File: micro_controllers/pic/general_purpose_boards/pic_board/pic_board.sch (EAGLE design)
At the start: 26 parts, among them IC1 PIC16f877a, IC2 7805TV

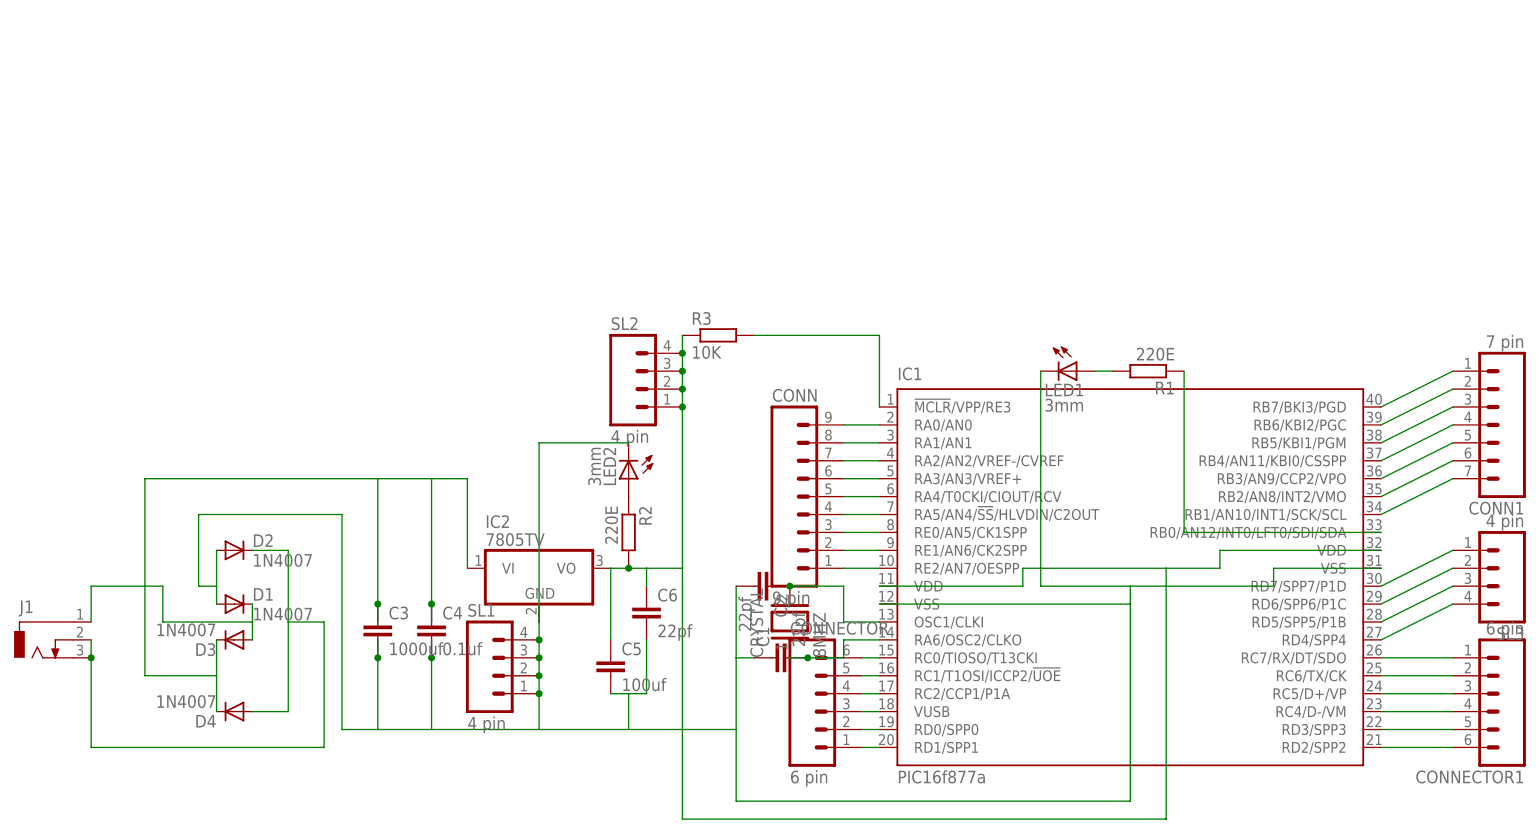
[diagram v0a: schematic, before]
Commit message: 
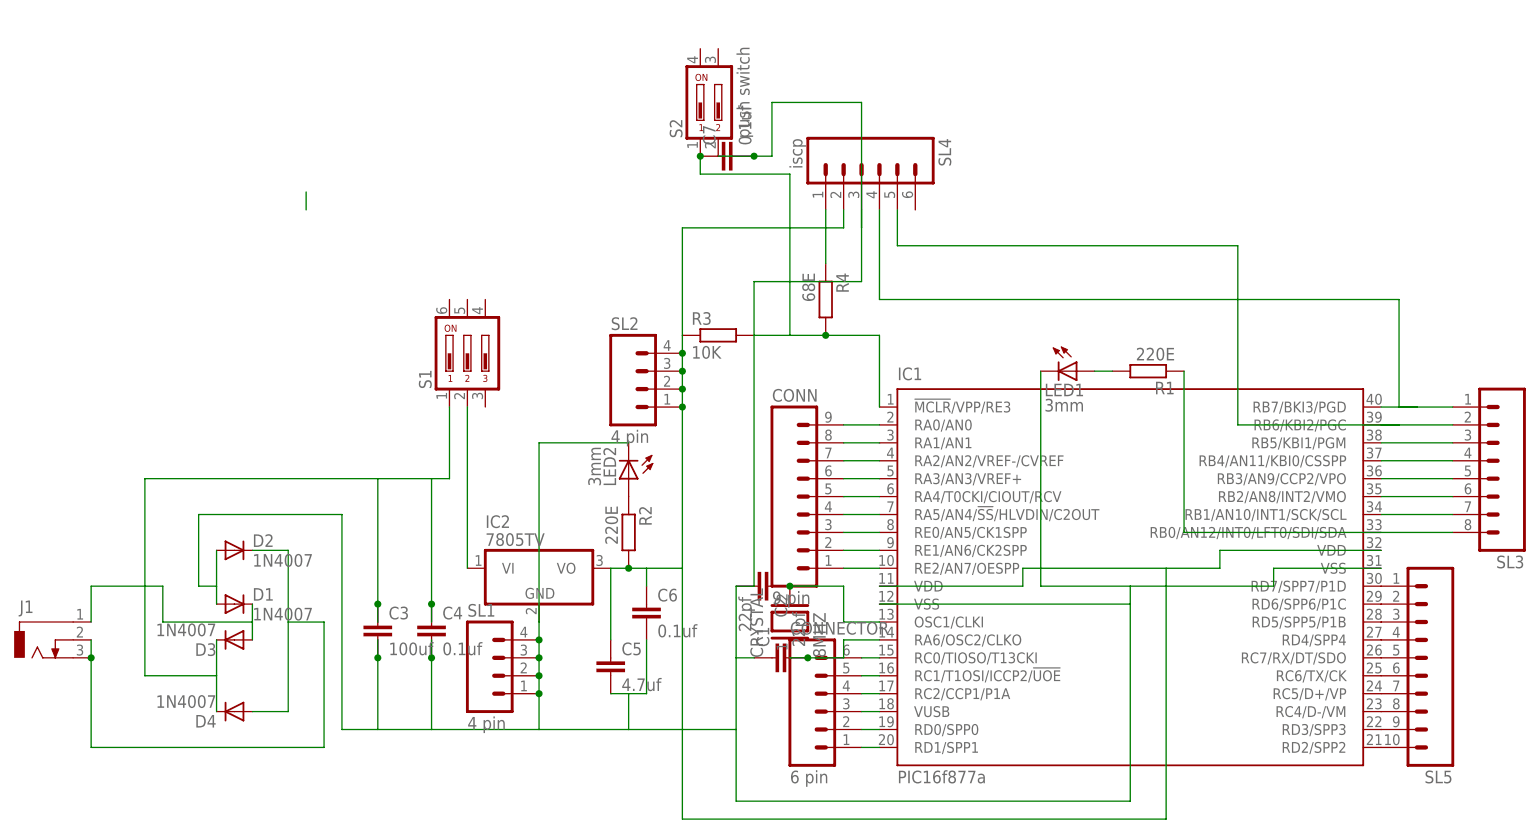
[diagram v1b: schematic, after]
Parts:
- removed CONN1: 7 pin, con-amp-quick:M07
- removed CONNECTOR1: 6 pin, con-amp-quick:M06
- added C7: 0.1uf, capacitor-wima:C2,5-3
- added R4: 68E, rcl:R-EU_0204/7
- added S1: (no value), switch-dil:DA03
- added S2: push switch, switch-dil:DP02
- added SL4: iscp, con-amp-quick:M06
- added SL5: (no value), con-amp-quick:M10
- C3: value 1000uf -> 100uf
- C5: value 100uf -> 4.7uf
- C6: value 22pf -> 0.1uf
- SL3: value 4 pin -> (none); device con-amp-quick:M04 -> con-amp-quick:M08; OC_FARNELL unknown -> (none); OC_NEWARK unknown -> (none)
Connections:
- new net N$44: R4.1, SL4.1
- new net N$45: IC2.VI, S1.2
- net N$19: now also SL3.1, SL4.4; no longer CONN1.1
- net N$20: now also SL3.2, SL4.5; no longer CONN1.2
- net N$21: now also SL3.3; no longer CONN1.3
- net N$22: now also SL3.4; no longer CONN1.4
- net N$23: now also SL3.5; no longer CONN1.5
- net N$24: now also SL3.6; no longer CONN1.6
- net N$25: now also SL3.7; no longer CONN1.7
- net N$26: now also IC1.RD7/SPP7/P1D, SL5.1; no longer CONNECTOR1.1, IC1.RC7/RX/DT/SDO
- net N$27: now also IC1.RD6/SPP6/P1C, SL5.2; no longer CONNECTOR1.2, IC1.RC6/TX/CK
- net N$28: now also IC1.RD5/SPP5/P1B, SL5.3; no longer CONNECTOR1.3, IC1.RC5/D+/VP
- net N$29: now also SL3.8
- net N$30: now also S1.1; no longer IC2.VI
- net N$33: now also SL4.2
- net N$35: now also C7.2, S2.2, SL4.3
- net N$36: now also IC1.RD4/SPP4, SL5.4; no longer CONNECTOR1.4, IC1.RC4/D-/VM
- net N$37: now also IC1.RC7/RX/DT/SDO, SL5.5; no longer CONNECTOR1.5, IC1.RD3/SPP3
- net N$38: now also IC1.RC6/TX/CK, SL5.6; no longer CONNECTOR1.6, IC1.RD2/SPP2
- net N$39: now also C7.1, R4.2, S2.1
- net N$40: now also IC1.RC5/D+/VP, SL5.7; no longer IC1.RD7/SPP7/P1D, SL3.1
- net N$41: now also IC1.RC4/D-/VM, SL5.8; no longer IC1.RD6/SPP6/P1C, SL3.2
- net N$42: now also IC1.RD3/SPP3, SL5.9; no longer IC1.RD5/SPP5/P1B, SL3.3
- net N$43: now also IC1.RD2/SPP2, SL5.10; no longer IC1.RD4/SPP4, SL3.4
